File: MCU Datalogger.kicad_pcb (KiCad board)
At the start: 2 copper layers, 29 parts, among them J1 Conn_01x04_Male, J2 Conn_01x09_Male, J3 Conn_01x04_Male, J4 Conn_02x03_Odd_Even, U1 24LC1025, U2 DS1337S+, U3 24LC1025, U4 ATMEGA328P-AU, Y1 32.768 KHz, Y2 16 MHz

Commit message: Setup Pcbnew.
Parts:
- moved BT1 11.6 mm to (220.3, 86.9)
- moved C1 11.6 mm to (213.8, 96.4)
- moved C3 11.6 mm to (214.3, 86.3)
- moved H1 11.6 mm to (219.1, 94.6)
- moved H3 11.6 mm to (230.3, 80.9)
- moved J1 11.6 mm to (255.4, 80.3)
- moved J2 11.6 mm to (246.1, 80.3)
- moved J3 11.6 mm to (250.8, 80.3)
- moved J4 11.6 mm to (260.1, 80.3)
- moved R3 11.6 mm to (235.4, 82.5)
- moved R4 11.6 mm to (235.1, 85.5)
- moved R5 11.6 mm to (229.3, 91.8)
- moved R6 11.6 mm to (230.6, 88.2)
- moved R7 11.6 mm to (224.9, 91.8)
- moved U1 11.6 mm to (212.8, 81.4)
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
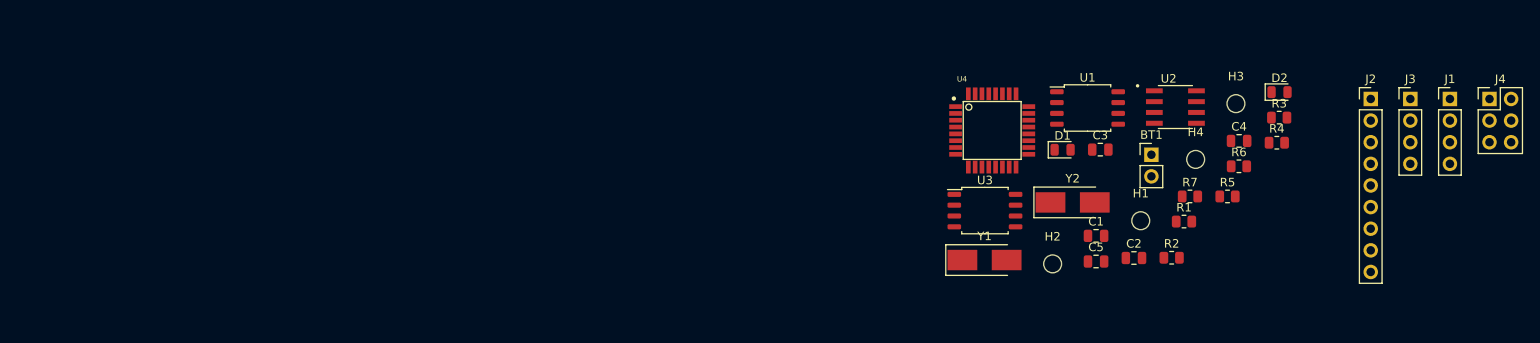
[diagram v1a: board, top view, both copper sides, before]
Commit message: Completed placement of footprints.
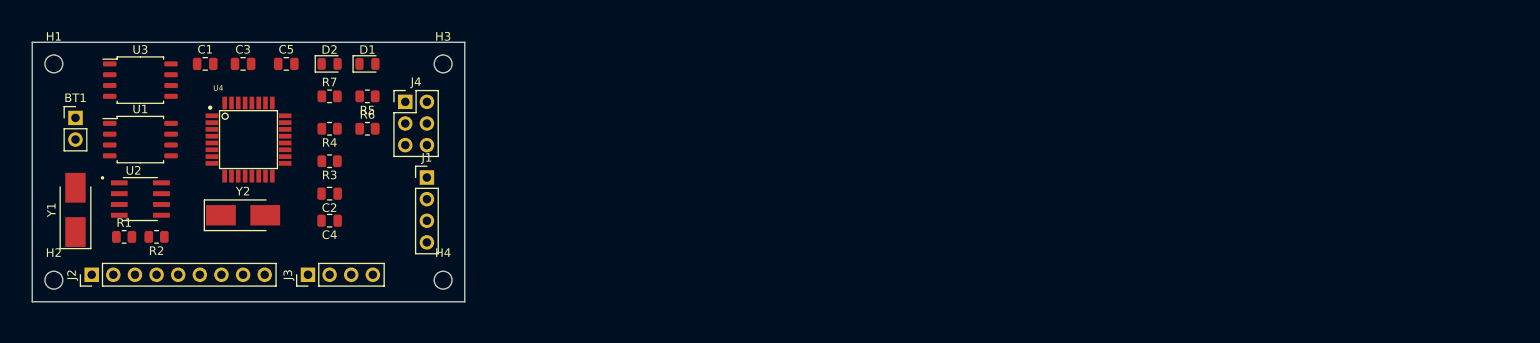
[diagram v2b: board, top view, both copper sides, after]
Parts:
- moved J2 151.6 mm to (95.9, 101.0), turned to 90 degrees
- moved J3 131.1 mm to (121.3, 101.0), turned to 90 degrees
- moved H1 129.0 mm to (91.4, 76.2)
- moved J4 127.3 mm to (132.7, 80.7)
- moved BT1 126.4 mm to (94.0, 82.5)
- moved R1 124.5 mm to (99.7, 96.5)
- moved U2 122.0 mm to (101.6, 92.1)
- moved J1 120.5 mm to (135.3, 89.5)
- moved R2 119.2 mm to (103.5, 96.5), turned to 180 degrees
- moved H2 117.3 mm to (91.4, 101.6)
- moved R3 111.6 mm to (123.8, 87.6), turned to 180 degrees
- moved D2 111.6 mm to (123.8, 76.2)
- moved U1 111.3 mm to (101.6, 85.1)
- moved R4 111.3 mm to (123.8, 83.8), turned to 180 degrees
- moved C4 107.2 mm to (123.8, 94.6), turned to 180 degrees
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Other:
- board outline added: 50.8 x 30.5 mm

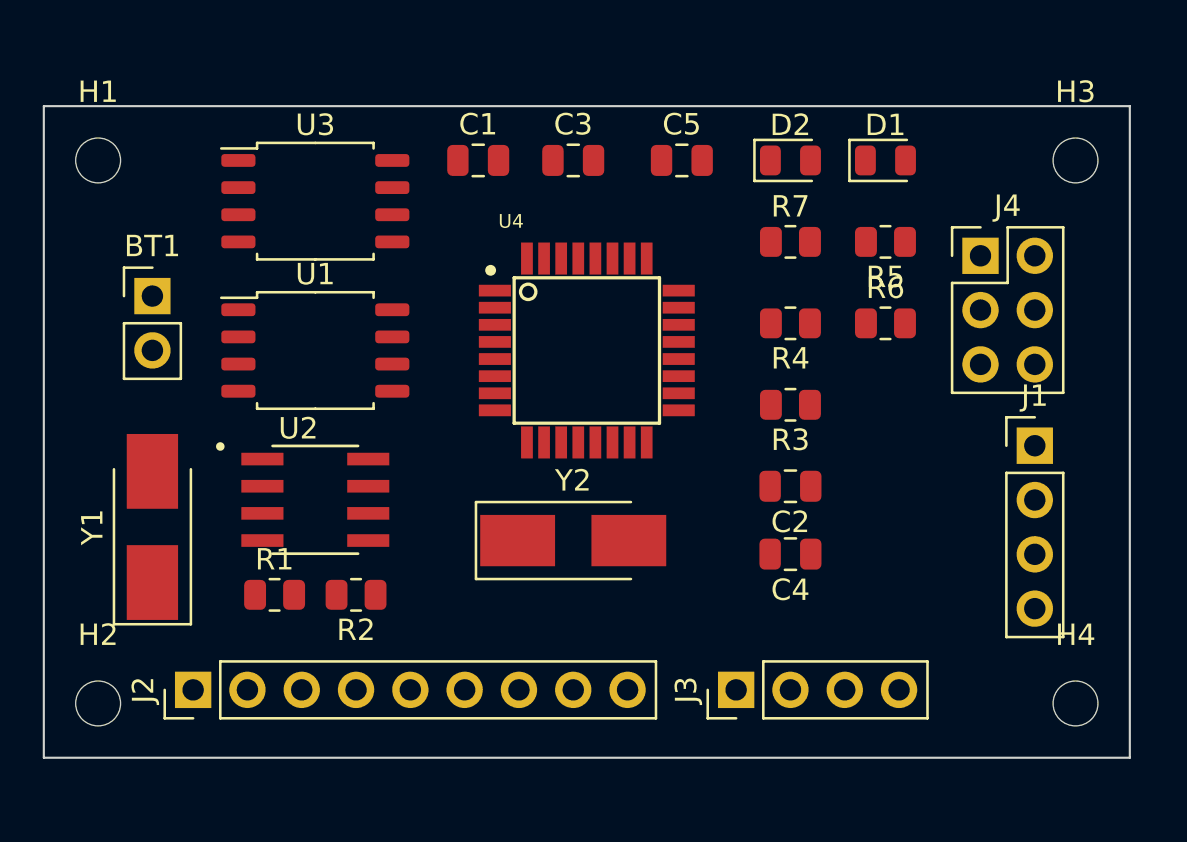
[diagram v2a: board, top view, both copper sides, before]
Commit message: Refined and completed outline.
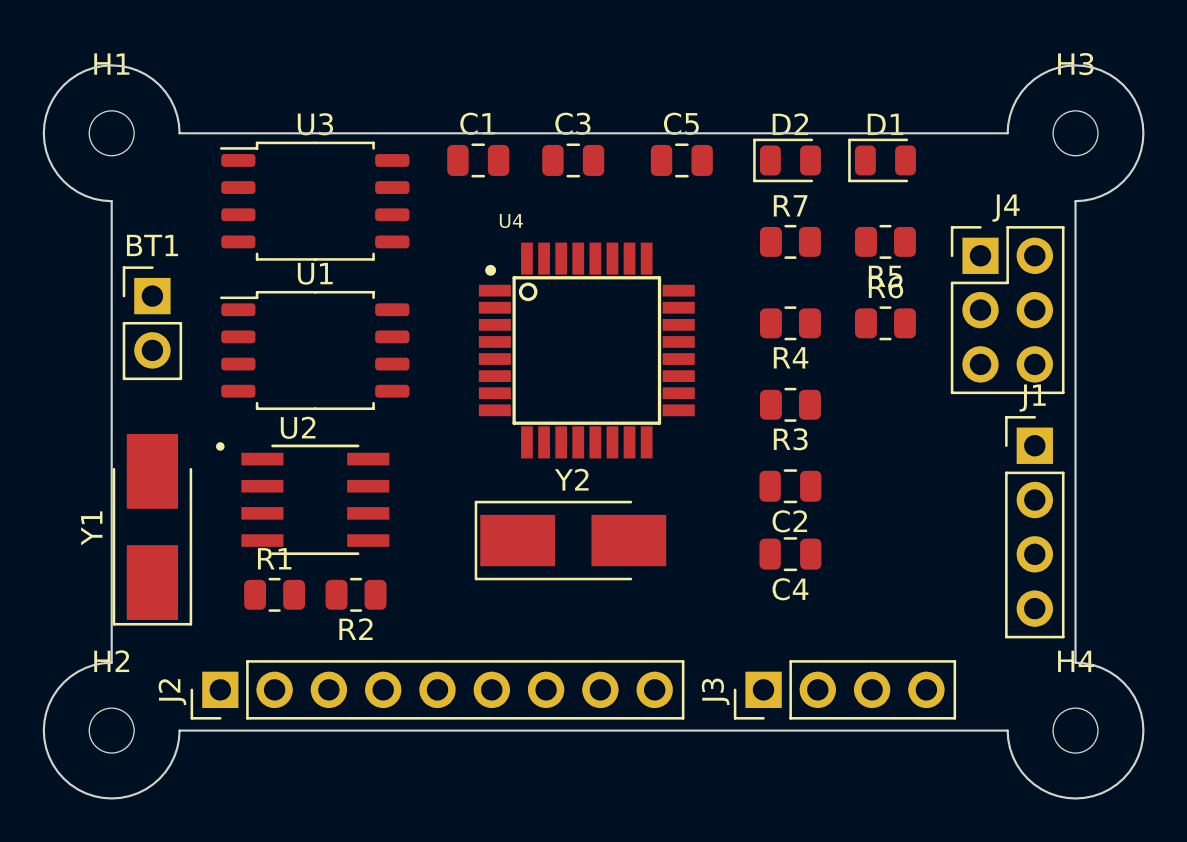
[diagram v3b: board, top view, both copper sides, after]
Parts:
- moved H2 1.42 mm to (92.1, 102.9)
- moved H1 1.42 mm to (92.1, 74.9)
- moved J3 1.28 mm to (122.6, 101.0)
- moved H4 1.27 mm to (137.2, 102.9)
- moved H3 1.27 mm to (137.2, 74.9)
- moved J2 1.27 mm to (97.2, 101.0)
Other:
- board size 50.8 x 30.5 mm -> 51.4 x 34.3 mm
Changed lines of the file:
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@@
   (net 35 "unconnected-(U4-Pad26)")
   (footprint "MountingHole:MountingHole_2.1mm" (layer "F.Cu")
-    (at 137.16 101.6)
+    (at 137.16 102.87)
     (descr "Mounting Hole 2.1mm, no annular")
     (tags "mounting hole 2.1mm no annular")
@@
   )
   (footprint "Connector_PinHeader_2.54mm:PinHeader_1x04_P2.54mm_Vertical" (layer "F.Cu")
-    (at 121.285 100.965 90)
+    (at 122.565 100.965 90)
     (descr "Through hole straight pin header, 1x04, 2.54mm pitch, single row")
     (tags "Through hole pin header THT 1x04 2.54mm single row")
@@
   )
   (footprint "MountingHole:MountingHole_2.1mm" (layer "F.Cu")
-    (at 91.44 76.2)
+    (at 92.075 74.93)
     (descr "Mounting Hole 2.1mm, no annular")
     (tags "mounting hole 2.1mm no annular")
@@
   )
   (footprint "MountingHole:MountingHole_2.1mm" (layer "F.Cu")
-    (at 91.44 101.6)
+    (at 92.075 102.87)
     (descr "Mounting Hole 2.1mm, no annular")
     (tags "mounting hole 2.1mm no annular")
@@
   )
   (footprint "MountingHole:MountingHole_2.1mm" (layer "F.Cu")
-    (at 137.16 76.2)
+    (at 137.16 74.93)
     (descr "Mounting Hole 2.1mm, no annular")
     (tags "mounting hole 2.1mm no annular")
@@
   )
   (footprint "Connector_PinHeader_2.54mm:PinHeader_1x09_P2.54mm_Vertical" (layer "F.Cu")
-    (at 95.885 100.965 90)
+    (at 97.155 100.965 90)
     (descr "Through hole straight pin header, 1x09, 2.54mm pitch, single row")
     (tags "Through hole pin header THT 1x09 2.54mm single row")
@@
     )
   )
-  (gr_rect (start 88.9 73.66) (end 139.7 104.14) (layer "Edge.Cuts") (width 0.1) (fill none))
+  (gr_arc (start 92.075 74.93) (end 95.25 74.93) (angle -270) (layer "Edge.Cuts") (width 0.1))
+  (gr_arc (start 137.16 74.93) (end 133.985 74.93) (angle 270) (layer "Edge.Cuts") (width 0.1))
+  (gr_line (start 137.16 99.695) (end 137.16 78.105) (layer "Edge.Cuts") (width 0.1))
+  (gr_arc (start 137.16 102.87) (end 137.16 99.695) (angle 270) (layer "Edge.Cuts") (width 0.1))
+  (gr_line (start 133.985 74.93) (end 95.25 74.93) (layer "Edge.Cuts") (width 0.1))
+  (gr_arc (start 92.075 102.87) (end 92.075 99.695) (angle -270) (layer "Edge.Cuts") (width 0.1))
+  (gr_line (start 92.075 78.105) (end 92.075 99.695) (layer "Edge.Cuts") (width 0.1))
+  (gr_line (start 95.25 102.87) (end 133.985 102.87) (layer "Edge.Cuts") (width 0.1))
 )

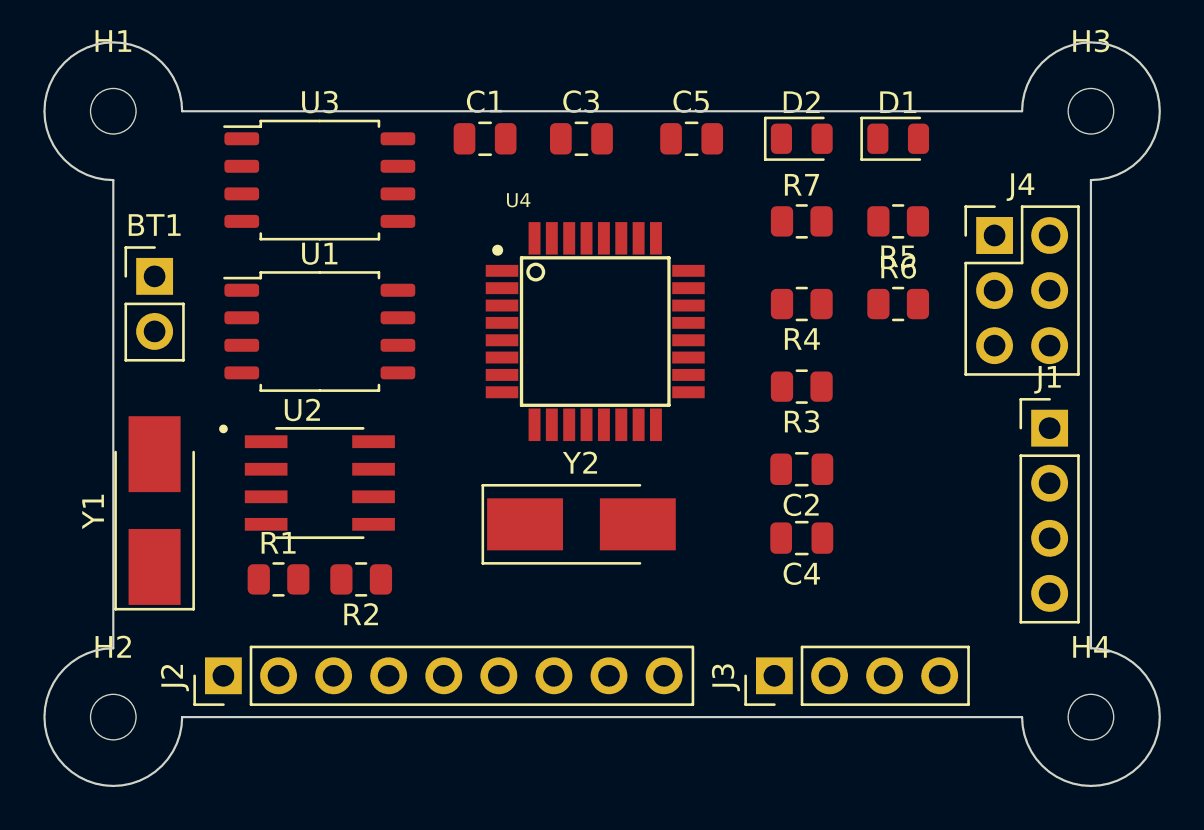
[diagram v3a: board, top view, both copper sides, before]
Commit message: Routing sans GND Vcc complete.
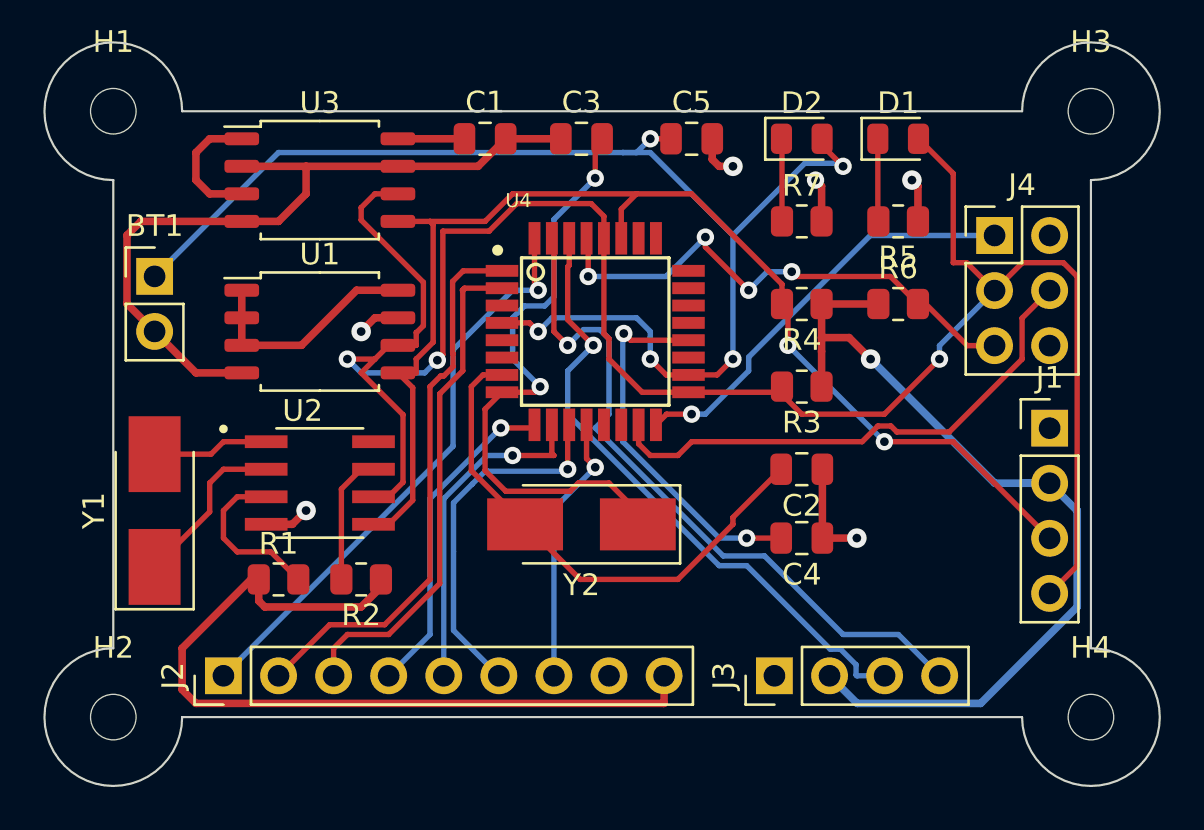
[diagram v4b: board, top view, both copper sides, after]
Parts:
- turned Y2 to 180 degrees
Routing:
- net /Vcc: track 0.00 -> 99.1 mm, vias 0 -> 1
- net /SCK: track 0.00 -> 97.2 mm, vias 0 -> 3
- net Net-(U4-Pad18): track 0.00 -> 60.2 mm, vias 0 -> 5
- net /SDA: track 0.00 -> 57.6 mm, vias 0 -> 2
- net GND: track 0.00 -> 50.6 mm, vias 0 -> 6
- net /TX: track 0.00 -> 32.6 mm, vias 0 -> 1
- net Net-(Y2-Pad1): track 0.00 -> 29.1 mm, vias 0 -> 2
- net /RX: track 0.00 -> 29.0 mm, vias 0 -> 1
- net /D2: track 0.00 -> 26.9 mm, vias 0 -> 1
- net /D3: track 0.00 -> 25.6 mm
- net /MOSI: track 0.00 -> 24.5 mm
- net /RESET: track 0.00 -> 24.3 mm, vias 0 -> 4
- net Net-(Y2-Pad2): track 0.00 -> 24.2 mm
- net /D4: track 0.00 -> 23.2 mm
- net /MISO: track 0.00 -> 19.6 mm, vias 0 -> 1
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
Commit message: Completed routing.
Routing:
- added copper zone on F.Cu, net /Vcc
- added copper zone on B.Cu, net GND
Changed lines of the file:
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@@
   (segment (start 93.98 95.945) (end 96.52 93.405) (width 0.25) (layer "F.Cu") (net 26))
   (segment (start 97.155 91.44) (end 99.125 91.44) (width 0.25) (layer "F.Cu") (net 26))
+  (zone (net 3) (net_name "/Vcc") (layer "F.Cu") (hatch edge 0.508)
+    (connect_pads (clearance 0.508))
+    (min_thickness 0.254) (filled_areas_thickness no)
+    (fill yes (mode hatch) (thermal_gap 0.508) (thermal_bridge_width 0.508)
+      (hatch_thickness 1.016) (hatch_gap 1.524) (hatch_orientation 0)
+      (hatch_border_algorithm hatch_thickness) (hatch_min_hole_area 0.3))
+    (polygon
+      (pts
+        (xy 136.906 78.232)
+        (xy 136.906 99.568)
+        (xy 133.858 102.616)
+        (xy 95.25 102.616)
+        (xy 92.202 99.568)
+        (xy 92.202 78.486)
+        (xy 95.504 75.184)
+        (xy 134.112 75.184)
+      )
+    )
+  )
+  (zone (net 2) (net_name "GND") (layer "B.Cu") (hatch edge 0.508)
+    (connect_pads (clearance 0.508))
+    (min_thickness 0.254) (filled_areas_thickness no)
+    (fill yes (mode hatch) (thermal_gap 0.508) (thermal_bridge_width 0.508)
+      (hatch_thickness 1.016) (hatch_gap 1.524) (hatch_orientation 0)
+      (hatch_border_algorithm hatch_thickness) (hatch_min_hole_area 0.3))
+    (polygon
+      (pts
+        (xy 136.906 78.232)
+        (xy 136.906 99.568)
+        (xy 133.858 102.616)
+        (xy 95.25 102.616)
+        (xy 92.202 99.568)
+        (xy 92.202 78.486)
+        (xy 95.504 75.184)
+        (xy 134.112 75.184)
+      )
+    )
+  )
 )

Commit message: Refined routing complete.
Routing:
- net GND: track 50.6 -> 85.4 mm, vias 6 -> 12
- net /Vcc: track 99.1 -> 119.4 mm, vias 1 -> 5
- net /D2: track 26.9 -> 30.9 mm
- net /D3: track 25.6 -> 27.3 mm, vias 0 -> 2
- net Net-(U4-Pad20): track 17.3 -> 18.4 mm
- net Net-(Y2-Pad2): track 24.2 -> 25.2 mm
- net /D4: track 23.2 -> 24.2 mm, vias 0 -> 2
- net /MOSI: track 24.5 -> 25.4 mm
- net /SDA: track 57.6 -> 58.3 mm
- net Net-(Y1-Pad1): track 7.79 -> 7.27 mm

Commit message: Fixed outstanding issues.
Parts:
- added G***: LOGO, DesktopLibrary:TE_Logo_11.6x4, B.Cu at (102.9, 85.0)
- added REF**: KiCad-Logo2_5mm_SilkScreen, Symbol:KiCad-Logo2_5mm_SilkScreen, B.Cu at (102.6, 78.6)
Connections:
- BT1 pad 1: Net-(U4-Pad18) -> /Vcc
- C5 pad 1: Net-(U4-Pad18) -> /Vcc
- D2 pad 2: Net-(U4-Pad18) -> /Vcc
- U4 pad 13: unconnected-(U4-Pad13) -> (no net)
- U4 pad 14: unconnected-(U4-Pad14) -> (no net)
- U4 pad 18: Net-(U4-Pad18) -> /Vcc
- U4 pad 19: unconnected-(U4-Pad19) -> (no net)
- U4 pad 22: unconnected-(U4-Pad22) -> (no net)
- U4 pad 23: unconnected-(U4-Pad23) -> (no net)
- U4 pad 24: unconnected-(U4-Pad24) -> (no net)
- U4 pad 25: unconnected-(U4-Pad25) -> (no net)
- U4 pad 26: unconnected-(U4-Pad26) -> (no net)
- U4 pad 4: Net-(U4-Pad18) -> /Vcc
- U4 pad 6: unconnected-(U4-Pad6) -> (no net)
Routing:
- net /Vcc: track 119.4 -> 188.4 mm, vias 5 -> 10
- net Net-(U4-Pad18): track 60.2 -> 0.00 mm, vias 5 -> 0
- net GND: track 85.4 -> 90.4 mm, vias 12 -> 13
- net /MISO: track 19.6 -> 20.2 mm
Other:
- board text added: "- 2Mbit EEPROM - RTC - I2C, SPI, GPIOs"
- board text added: "2"
- board text added: "3"
- board text added: "4"
- board text added: "5"
- board text added: "6"
- board text added: "7"
- board text added: "8"
- board text added: "Data logger with the ATMega328P."
- board text added: "GND"
- board text added: "GPIO"
- board text added: "I2C"
- board text added: "ICSP"
- board text added: "ICSP MISO | VCC SCK | MOSI RESET| GND"
- board text added: "RX"
- board text added: "SCK"
- board text added: "SDA"
- board text added: "SERIAL"
- board text added: "TX"
- board text added: "VCC"
